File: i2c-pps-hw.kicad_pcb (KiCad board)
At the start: 4 copper layers, 95 x 60 mm, 121 parts, among them J1 +5V, J2 Vout, J3 Digital I/O, Q1 SiR880BDP, Q2 SiR880BDP, Q3 SiR880BDP, Q4 SiR880BDP, Q5 SIS413DN, Q6 MMBT3904, Q7 MMBT3904, Q8 SIS413DN, U1 BQ25758S, U2 AP2210-3.3, U3 74AHC1G14

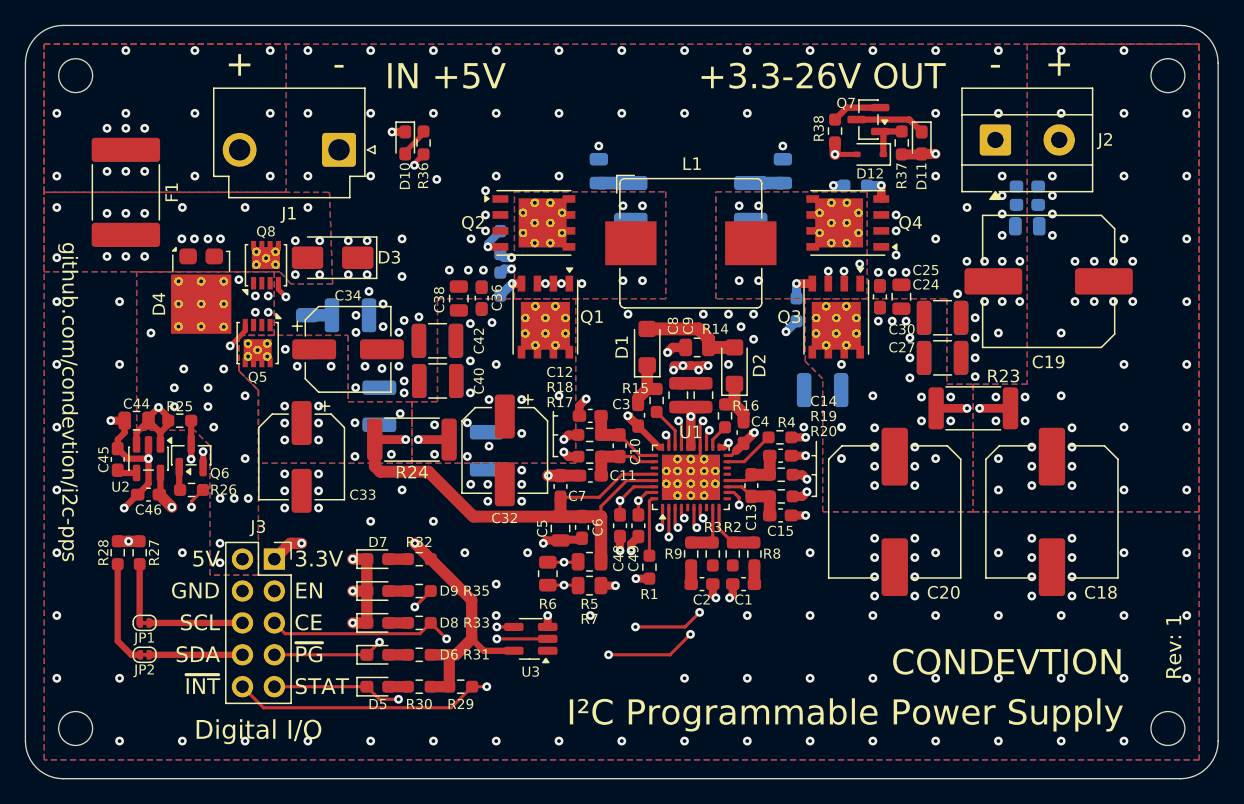
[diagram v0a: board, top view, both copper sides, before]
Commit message: Add more vias
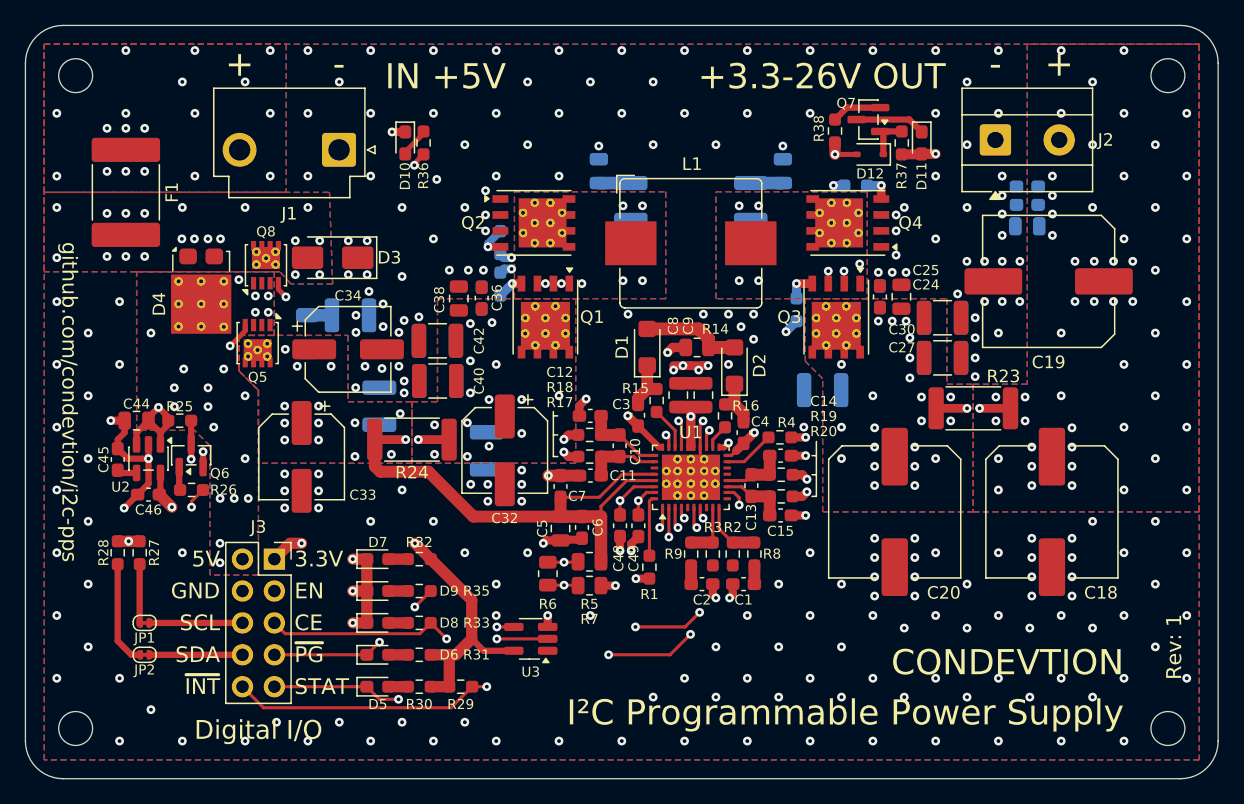
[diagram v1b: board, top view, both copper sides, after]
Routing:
- net /Digital IO and Indication/+5V_Prot: track 30.5 -> 29.9 mm
- net GND: vias 204 -> 250
- net /Master Switch/+5V: vias 16 -> 18
- net /Controller and Power Stage/VOUT_Filtered: vias 47 -> 56

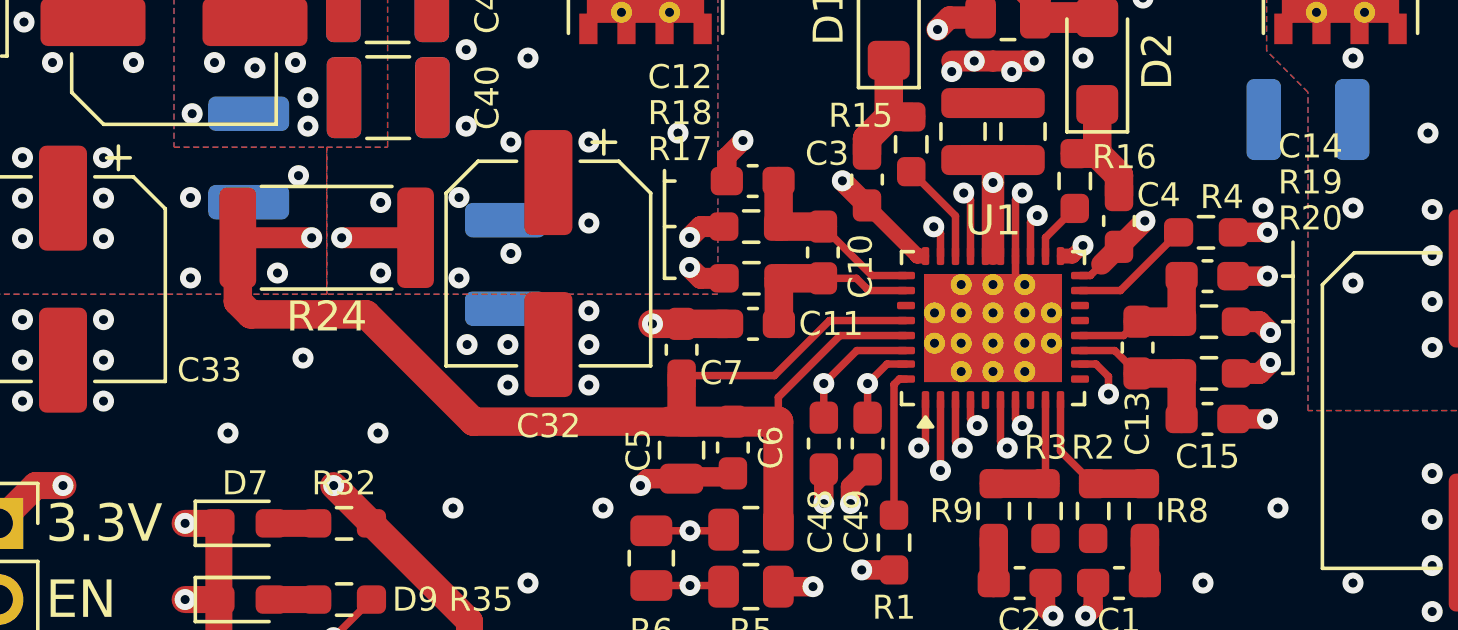
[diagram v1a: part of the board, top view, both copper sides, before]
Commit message: Adjust vias, GND top zone, and setup fabrication output
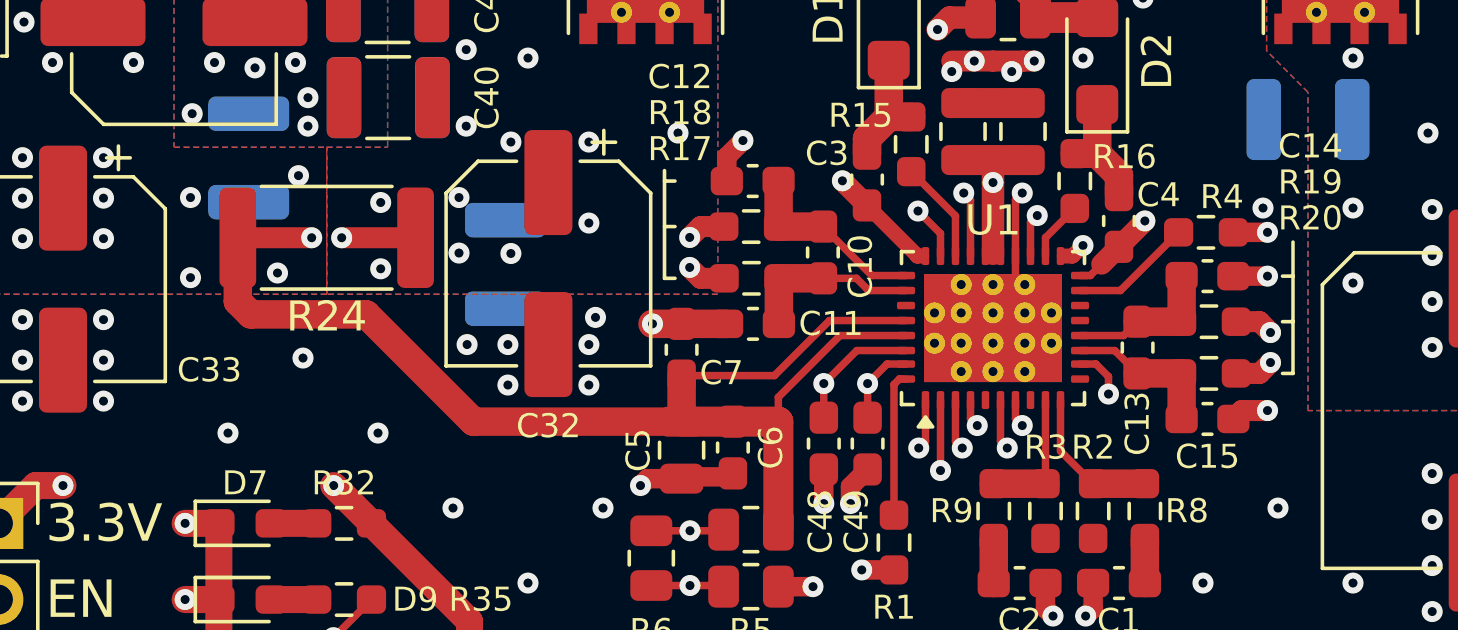
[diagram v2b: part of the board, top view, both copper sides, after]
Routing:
- net /Controller and Power Stage/VOUT_Filtered: track 98.0 -> 100.7 mm
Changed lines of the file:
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@@
 			(disableapertmacros no)
 			(usegerberextensions no)
-			(usegerberattributes yes)
-			(usegerberadvancedattributes yes)
+			(usegerberattributes no)
+			(usegerberadvancedattributes no)
 			(creategerberjobfile yes)
 			(dashed_line_dash_ratio 12.000000)
@@
 			(outputformat 1)
 			(mirror no)
-			(drillshape 1)
+			(drillshape 0)
 			(scaleselection 1)
-			(outputdirectory "")
+			(outputdirectory "gerber/")
 		)
 	)
@@
 	)
 	(segment
+		(start 146.2925 111.75)
+		(end 146.0125 112.03)
+		(width 0.7)
+		(layer "F.Cu")
+		(net 2)
+	)
+	(segment
 		(start 92.3525 106.7075)
 		(end 93.155 107.51)
@@
 	)
 	(segment
-		(start 147.15 112.03)
-		(end 146.0125 112.03)
-		(width 0.65)
-		(layer "F.Cu")
-		(net 2)
-	)
-	(segment
 		(start 92.9025 104.48)
 		(end 91.8025 104.48)
@@
 		(net 2)
 	)
+	(segment
+		(start 147.15 111.75)
+		(end 146.2925 111.75)
+		(width 0.7)
+		(layer "F.Cu")
+		(net 2)
+	)
 	(via
 		(at 111.07 120.59)
@@
 	)
 	(via
-		(at 147.15 112.03)
+		(at 147.15 111.75)
 		(size 0.7)
 		(drill 0.3)
@@
 	)
 	(via
-		(at 124.53 108.425)
+		(at 124.75 108.645)
 		(size 0.7)
 		(drill 0.3)
@@
 	)
 	(via
-		(at 111.25 107.33)
+		(at 111.25 107.32)
 		(size 0.7)
 		(drill 0.3)
@@
 	)
 	(segment
-		(start 165.34 84.12)
-		(end 167.34 82.12)
+		(start 157.465 111.085)
+		(end 160.73 107.82)
 		(width 0.25)
 		(layer "In2.Cu")
@@
 	)
 	(segment
-		(start 157.465 111.085)
-		(end 160.73 107.82)
+		(start 166.25 81.03)
+		(end 166.25 79.74)
 		(width 0.25)
 		(layer "In2.Cu")
@@
 	)
 	(segment
-		(start 158.385 84.12)
-		(end 165.34 84.12)
+		(start 167.34 82.12)
+		(end 166.25 81.03)
 		(width 0.25)
 		(layer "In2.Cu")
@@
 	)
 	(segment
-		(start 157.5 83.235)
-		(end 158.385 84.12)
-		(width 0.25)
-		(layer "In2.Cu")
-		(net 16)
-	)
-	(segment
 		(start 168.605 83.385)
 		(end 168.605 89.875)
@@
 	)
 	(segment
+		(start 161.845 78.89)
+		(end 157.5 83.235)
+		(width 0.25)
+		(layer "In2.Cu")
+		(net 16)
+	)
+	(segment
+		(start 165.4 78.89)
+		(end 161.845 78.89)
+		(width 0.25)
+		(layer "In2.Cu")
+		(net 16)
+	)
+	(segment
+		(start 166.25 79.74)
+		(end 165.4 78.89)
+		(width 0.25)
+		(layer "In2.Cu")
+		(net 16)
+	)
+	(segment
 		(start 146.1125 108.7875)
 		(end 146.8875 108.7875)
@@
 	)
 	(via
-		(at 120.2 107.33)
+		(at 120.2 106.5)
 		(size 0.7)
 		(drill 0.3)
@@
 	)
 	(via
-		(at 117.59 107.165)
+		(at 117.59 107.025)
 		(size 0.7)
 		(drill 0.3)
@@
 	)
 	(segment
-		(start 136.25 106.6)
-		(end 136.25 105.85)
+		(start 136.25 105.85)
+		(end 135.5 105.1)
 		(width 0.25)
 		(layer "F.Cu")
@@
 	)
 	(segment
-		(start 136.25 105.85)
-		(end 136.025 105.625)
+		(start 136.25 106.6)
+		(end 136.25 105.85)
 		(width 0.25)
 		(layer "F.Cu")
@@
 	)
 	(via
-		(at 136.025 105.625)
+		(at 135.5 105.1)
 		(size 0.7)
 		(drill 0.3)
@@
 	)
 	(segment
-		(start 130.35 99.95)
-		(end 130.35 93.16)
+		(start 130.35 93.16)
+		(end 129.59 92.4)
 		(width 0.7)
 		(layer "In2.Cu")
@@
 	)
 	(segment
-		(start 129.59 92.4)
-		(end 123.72 92.4)
+		(start 130.35 99.95)
+		(end 130.35 93.16)
 		(width 0.7)
 		(layer "In2.Cu")
@@
 	)
 	(segment
-		(start 130.35 93.16)
-		(end 129.59 92.4)
+		(start 135.5 105.1)
+		(end 130.35 99.95)
 		(width 0.7)
 		(layer "In2.Cu")
@@
 	)
 	(segment
-		(start 136.025 105.625)
-		(end 130.35 99.95)
+		(start 129.59 92.4)
+		(end 123.72 92.4)
 		(width 0.7)
 		(layer "In2.Cu")
@@
 			)
 		)
+	)
+	(zone
+		(net 0)
+		(net_name "")
+		(layer "F.Cu")
+		(hatch edge 0.5)
+		(connect_pads
+			(clearance 0)
+		)
+		(min_thickness 0.25)
+		(filled_areas_thickness no)
+		(keepout
+			(tracks allowed)
+			(vias allowed)
+			(pads allowed)
+			(copperpour not_allowed)
+			(footprints allowed)
+		)
+		(placement
+			(enabled no)
+			(sheetname "")
+		)
+		(fill
+			(thermal_gap 0.5)
+			(thermal_bridge_width 0.5)
+		)
+		(polygon
+			(pts
+				(xy 135.65 107.15) (xy 140.35 107.15) (xy 140.35 110.85) (xy 135.65 110.85)
+			)
+		)
